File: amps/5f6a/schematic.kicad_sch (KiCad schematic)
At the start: 64 parts, among them T3 2R sec

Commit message: Fix: schematic wiring on the tweed family, jtm45 and 6161
- pot cold lugs: s.gnd() sat 3.81 mm below cx:POT pin 3 on nine sheets
  (19 pins); every flag now lands on the lug
- retyped coordinates replaced by helper returns (5e5a OT pins alone freed
  nine pins; 5d3 V3 cathode, 5f10 RKB, 5e6a CBS, 5f2a dropper, grid leaks)
- shorts only verify_schematic_nets could see: 5e3 cathode bus through V4's
  screen pin (B+2 tied to the cathodes), C7 through RG6A, PI leak through
  RGPI, C8 on the cathode not the tail; 5f10 the same RGPI/C7 pair; 5e5a
  presence feed down the tube column; 5e6a RFB loop through RL3
- three dated waivers: two-terminal rheostat far lugs (5e6a VR5, 6161 VR3/VR4)

Co-Authored-By: Claude Fable 5.1 <noreply@anthropic.com>
Claude-Session: https://claude.ai/code/session_01KBMfdh37HmCL2iWcBiL5J1
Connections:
- net GND: now also VR1.3, VR2.3
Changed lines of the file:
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@@
   (symbol (lib_id "cx:POT") (at 67.2688 30.988 0) (unit 1)
     (in_bom yes) (on_board yes)
-    (property "Reference" "VR1" (at 66.2528 35.328 0) (effects (font (size 1.27 1.27)) (justify left)))
-    (property "Value" "1M vol" (at 66.2528 37.728 0) (effects (font (size 1.27 1.27)) (justify left))))
-  (global_label "GND" (shape input) (at 67.2688 38.608 270)
+    (property "Reference" "VR1" (at 52.5476 29.348 0) (effects (font (size 1.27 1.27)) (justify left)))
+    (property "Value" "1M vol" (at 52.5476 31.748 0) (effects (font (size 1.27 1.27)) (justify left))))
+  (global_label "GND" (shape input) (at 67.2688 34.798 270)
     (effects (font (size 1.27 1.27)) (justify right)))
   (wire (pts (xy 72.3488 30.988) (xy 74.8888 30.988))
@@
     (property "Reference" "VR2" (at 59.1476 63.348 0) (effects (font (size 1.27 1.27)) (justify left)))
     (property "Value" "1M vol" (at 59.1476 65.748 0) (effects (font (size 1.27 1.27)) (justify left))))
-  (global_label "GND" (shape input) (at 67.2688 72.608 270)
+  (global_label "GND" (shape input) (at 67.2688 68.798 270)
     (effects (font (size 1.27 1.27)) (justify right)))
   (wire (pts (xy 72.3488 64.988) (xy 74.8888 64.988))

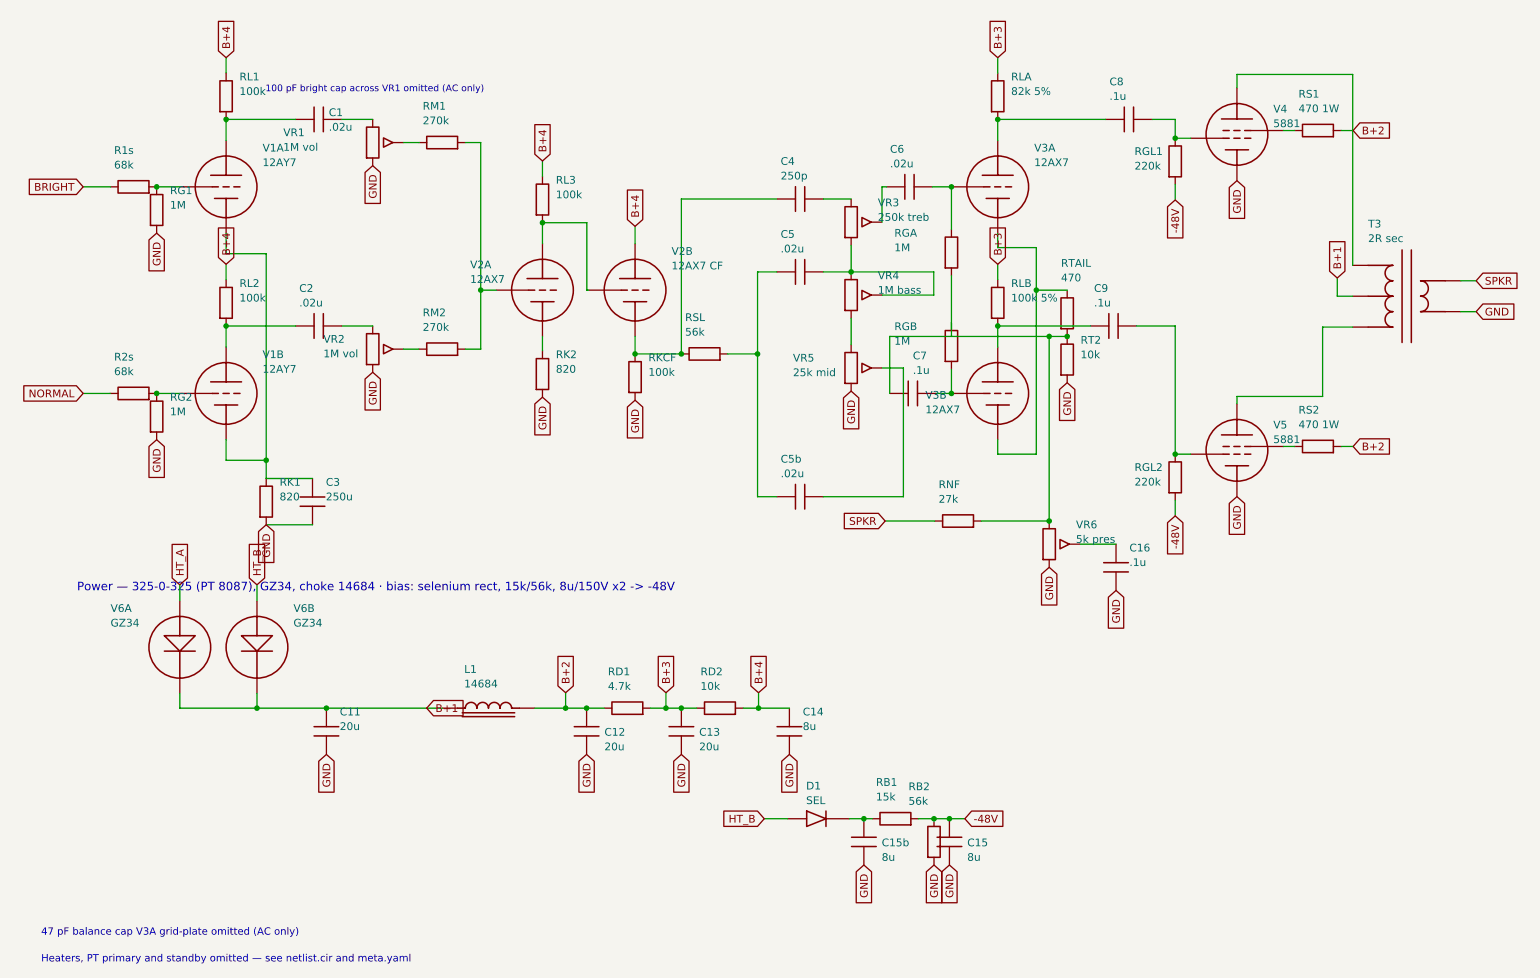
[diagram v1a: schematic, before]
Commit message: Add: real tube pin numbers and readable valve glyphs on every schematic
Phase B of the drawing program. A factory service sheet numbers every tube
pin, because the number is what a technician puts a probe on. This corpus
printed none, and the numbers hidden in its symbols were positional
placeholders (P=1, G=2, K=3) that would have published a 6V6GT's plate as
pin 1 when it is pin 3.

1055 electrodes now carry the real number, 1027 lettered (27 are shared
filaments deduped, 1 dropped for want of clear space on the 6G2). Resolved per
instance from reference/tubes/<slug>.yaml through the same alias resolution the
layout renderer uses, so a 12AX7 section and a 6SL7 section each get their own
basing. A valve whose basing the corpus does not carry prints nothing rather
than a wrong number.

Section letters and basing units are now separate things, which cost a detour
worth recording. The RCA 12AX7-A sheet reads "Pin 1 - Plate of Unit No.2 ...
Pin 6 - Plate of Unit No.1", so unit numbering is not pin order; the 5Y3 and
GZ34 number their units in opposite pin order, so nothing positional can
express it. But the section LETTER is a designator, not a basing fact: this
corpus, like every technician, calls the first stage in signal order V1A, and
five amps' prose already did. On four amps the factory sheets put that first
stage on the other half -- the AA764's own schematic prints +200 V on pin 1 --
so those drawings now state their unit explicitly, each citing its source, and
no letter, netlist, parts list or layout comment changed. 183 layout comments
agree with the printed numbers, 0 disagree. A guard fires if two halves of one
bottle resolve to the same unit, which is exactly how this was found.

Glyphs: the cathode gains a bracket and filament hairpin so it can no longer be
confused with the plate bar, the pentode's screen sits on its own row, and a
rectifier draws as one envelope over its sections instead of two apparent
bottles. Line weights are scaled per sheet to a co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
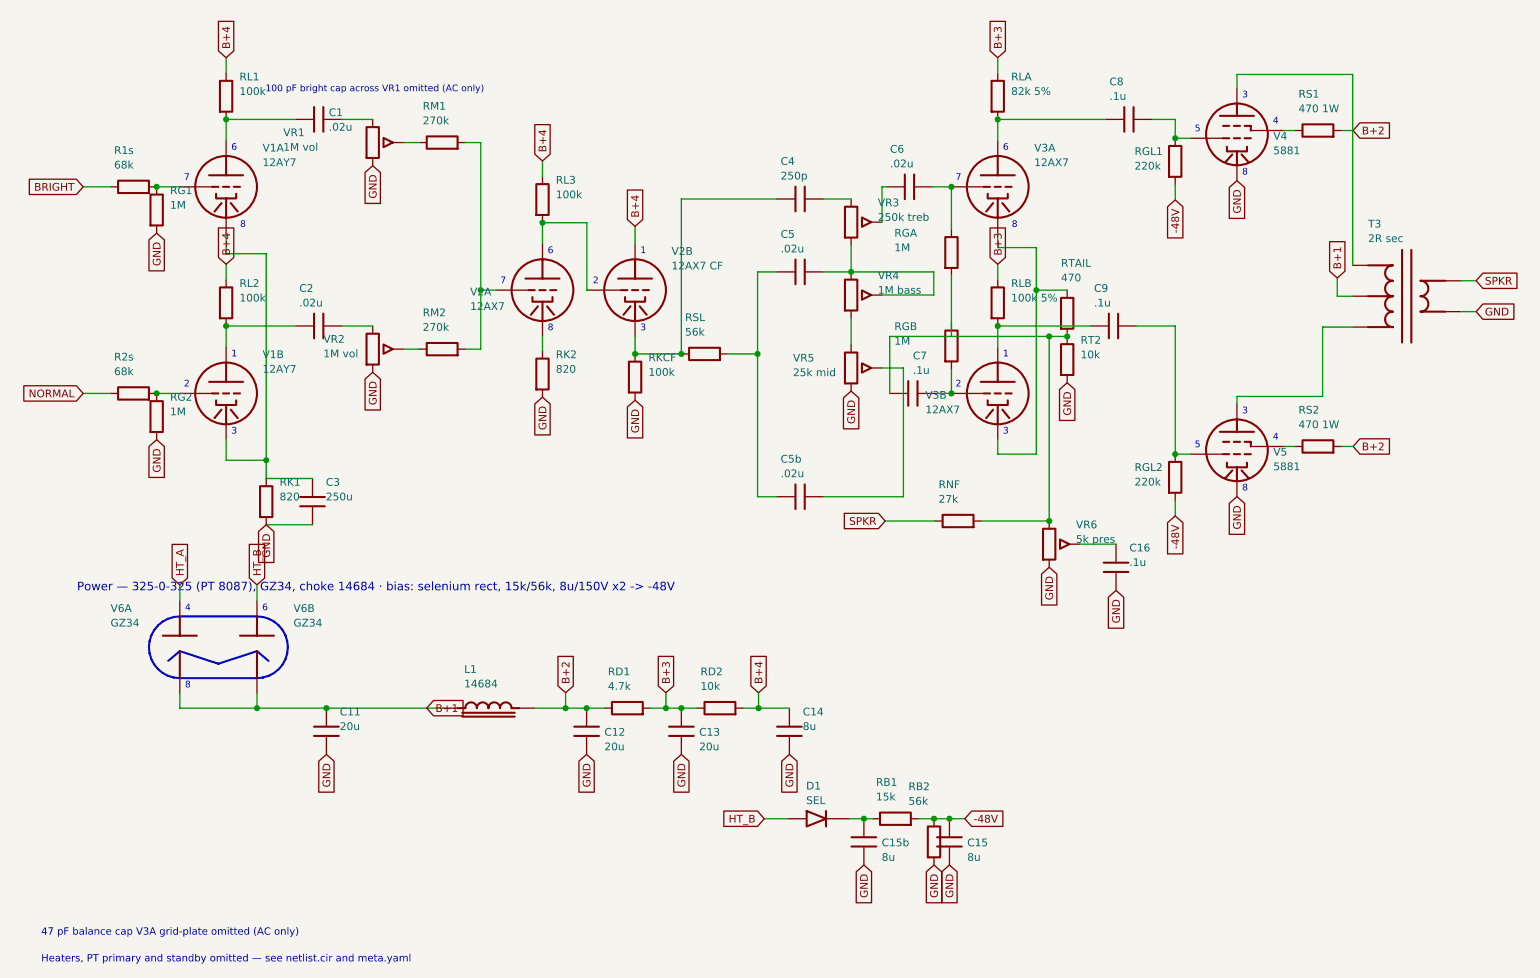
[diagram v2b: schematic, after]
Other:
- note added: "1"
- note added: "2"
- note added: "3"
- note added: "4"
- note added: "5"
- note added: "6"
- note added: "7"
- note added: "8"

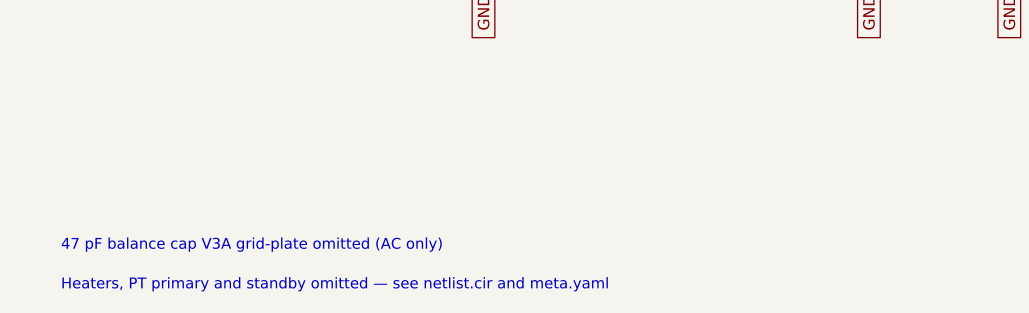
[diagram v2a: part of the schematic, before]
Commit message: Fix: schematic sheet notes no longer name repository files
Thirty-seven committed sheets rendered footnotes and section notes such as
"Heaters and PT primary omitted — see netlist.cir and meta.yaml" or
"excluded from netlist.cir (notes.md)" to visitors through KiCanvas. The
prose sweeps never counted sheets. Rewritten in the site's own words — the
netlist, the sources list, the circuit story, the parts list, the board
drawing — in 59 strings across 33 draw scripts, keeping every technical
claim as it was; the three tone sheets (6G4, 6G5, 6G6-B) are under repair
elsewhere and keep theirs for now. The sweep touched only strings passed to
the sheet's note, text, caption and footnote calls, never a path or a value.

Gates: check_schematics 40/0, connectivity 0 isolated pins;
verify_schematic_nets 40 clean; only the regenerated sheets and their served
copies changed.

Co-Authored-By: Claude Fable 5.1 <noreply@anthropic.com>
Claude-Session: https://claude.ai/code/session_01KBMfdh37HmCL2iWcBiL5J1
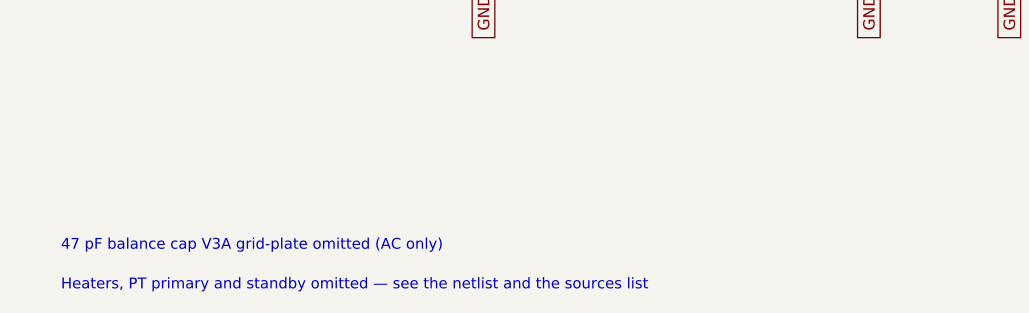
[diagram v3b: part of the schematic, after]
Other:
- note added: "Heaters, PT primary and standby omitted — see the netlist and the sources list"
- note removed: "Heaters, PT primary and standby omitted — see netlist.cir and meta.yaml"
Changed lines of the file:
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@@
   (text "47 pF balance cap V3A grid-plate omitted (AC only)" (at 12.7 161.056 0)
     (effects (font (size 1.2 1.2)) (justify left)))
-  (text "Heaters, PT primary and standby omitted — see netlist.cir and meta.yaml" (at 12.7 165.456 0)
+  (text "Heaters, PT primary and standby omitted — see the netlist and the sources list" (at 12.7 165.456 0)
     (effects (font (size 1.2 1.2)) (justify left)))
   (sheet_instances (path "/" (page "1")))

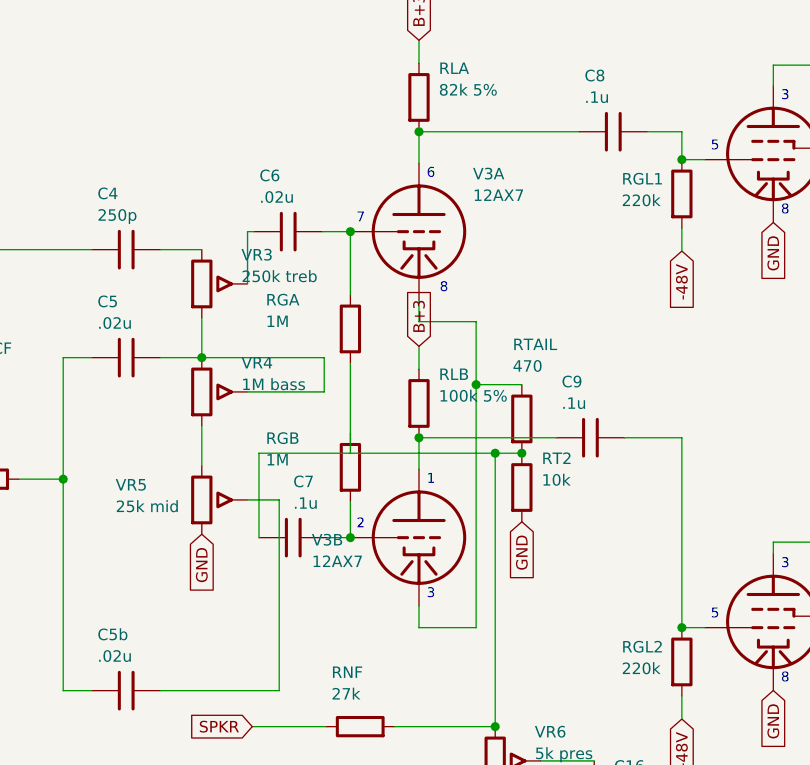
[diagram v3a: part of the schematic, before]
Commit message: Fix: six sheets letter valve sections and bias rows the way their factory drawings do
Sections — the board was right and the sheet printed the other half's pin
numbers (triage verdict rows, crops under the triage scratch):
  AC30 V1    JMI OS/065 (3600x2492): Brilliant grid 2 / plate 1, Normal 7 / 6
  AA964 V1   input 2/1/3, second stage 7/6/8 (6322x3926)
  AA964 V2   phase inverter 7/6/8, tremolo oscillator 2/1/3
  5F6-A V3   the 82k (input) triode on 1/2/3 on the I-EG layout (6402x3641)
  6G4 V5     the 82k triode on 1/2/3 on the A-FJ layout (2250x1269, the only copy)

Bias rows — the 5F4 (C-EG) and 5E4-A (G-EE) drawings run the series
resistor (6800 / 18K) from the transformer's bias tap INTO the selenium
rectifier. The previous commit's rows put the rectifier on the tap and the
resistor after it; both now read tap -> resistor -> rectifier -> node. The
5F4 rectifier sits clear of C17's ground flag.

Worklist after re-export: section swaps 10 -> 5 (three board re-pins in
flight, the 5E5-A whose only copy does not resolve, and the AA1164 V4 still
being read); the 5F4/5E4-A D1 rows stay MISPLACED until their boards take
the tap lead, which the board repair wave is adding.

Gates: check_schematics 40/0 (+selftest), verify_schematic_nets 40 clean,
tone gate, validate, check_value_consistency --strict 0, test_era_values,
verify_sheet_vs_board selftest 19 + drift clean after --export,
check_heaters, verify_layout_nets; regenerating every sheet changes only
these six.

Co-Authored-By: Claude Opus 5 (1M context) <noreply@anthropic.com>
Claude-Session: https://claude.ai/code/session_01KBMfdh37HmCL2iWcBiL5J1
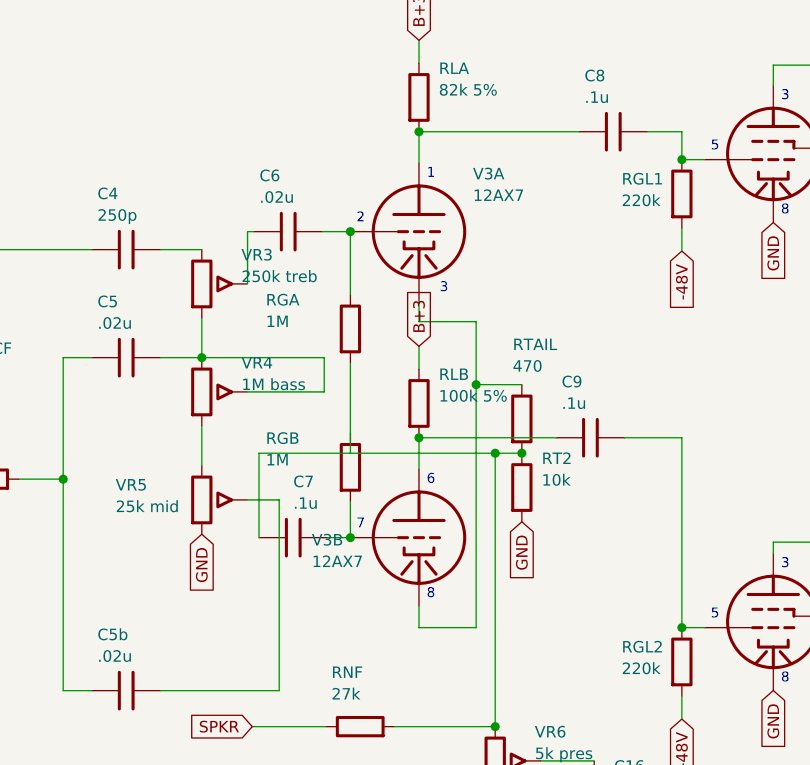
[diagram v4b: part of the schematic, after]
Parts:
- V3A: Basing_unit (none) -> 2
- V3B: Basing_unit (none) -> 1
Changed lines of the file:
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@@
     (in_bom yes) (on_board yes)
     (property "Reference" "V3A" (at 176.139 31.878 0) (effects (font (size 1.27 1.27)) (justify left)))
-    (property "Value" "12AX7" (at 176.139 34.278 0) (effects (font (size 1.27 1.27)) (justify left))))
+    (property "Value" "12AX7" (at 176.139 34.278 0) (effects (font (size 1.27 1.27)) (justify left)))
+    (property "Basing_unit" "2" (at 176.139 36.678 0) (effects (font (size 1.27 1.27)) hide)))
   (wire (pts (xy 162.519 38.278) (xy 162.519 38.278))
     (stroke (width 0) (type default)))
@@
     (in_bom yes) (on_board yes)
     (property "Reference" "V3B" (at 158.234 72.558 0) (effects (font (size 1.27 1.27)) (justify left)))
-    (property "Value" "12AX7" (at 158.234 74.958 0) (effects (font (size 1.27 1.27)) (justify left))))
+    (property "Value" "12AX7" (at 158.234 74.958 0) (effects (font (size 1.27 1.27)) (justify left)))
+    (property "Basing_unit" "1" (at 158.234 77.358 0) (effects (font (size 1.27 1.27)) hide)))
   (wire (pts (xy 170.139 30.658) (xy 170.139 27.178))
     (stroke (width 0) (type default)))
@@
   (text "3" (at 111.299 61.628 0)
     (effects (font (size 1.1 1.1)) (justify left)))
-  (text "6" (at 170.989 31.928 0)
-    (effects (font (size 1.1 1.1)) (justify left)))
-  (text "7" (at 163.192 36.878 0)
-    (effects (font (size 1.1 1.1)) (justify left)))
-  (text "8" (at 172.439 44.628 0)
-    (effects (font (size 1.1 1.1)) (justify left)))
-  (text "1" (at 170.989 65.928 0)
-    (effects (font (size 1.1 1.1)) (justify left)))
-  (text "2" (at 163.192 70.878 0)
-    (effects (font (size 1.1 1.1)) (justify left)))
-  (text "3" (at 170.989 78.628 0)
+  (text "1" (at 170.989 31.928 0)
+    (effects (font (size 1.1 1.1)) (justify left)))
+  (text "2" (at 163.192 36.878 0)
+    (effects (font (size 1.1 1.1)) (justify left)))
+  (text "3" (at 172.439 44.628 0)
+    (effects (font (size 1.1 1.1)) (justify left)))
+  (text "6" (at 170.989 65.928 0)
+    (effects (font (size 1.1 1.1)) (justify left)))
+  (text "7" (at 163.192 70.878 0)
+    (effects (font (size 1.1 1.1)) (justify left)))
+  (text "8" (at 170.989 78.628 0)
     (effects (font (size 1.1 1.1)) (justify left)))
   (text "3" (at 210.359 23.293 0)
